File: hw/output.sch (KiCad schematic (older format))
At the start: 44 parts, among them J401 Conn_01x02, J402 Conn_01x02, J403 Conn_01x02, J404 Conn_01x02, J405 Conn_01x02, J406 Conn_01x02, J407 Conn_01x02, J408 Conn_01x02, J409 SERVO_OUT, J410 AUDIO, Q401 IRLML6344TRPBF, Q402 IRLML6344TRPBF, Q403 IRLML6344TRPBF, Q404 CSD17306Q5A, Q405 IRLML6344TRPBF, Q406 IRLML6344TRPBF, Q407 IRLML6344TRPBF, Q408 CSD17306Q5A, U401 MCP1416, U402 MCP1416, U403 AD5160BRJZ10-R2, U404 MCP6001-OT

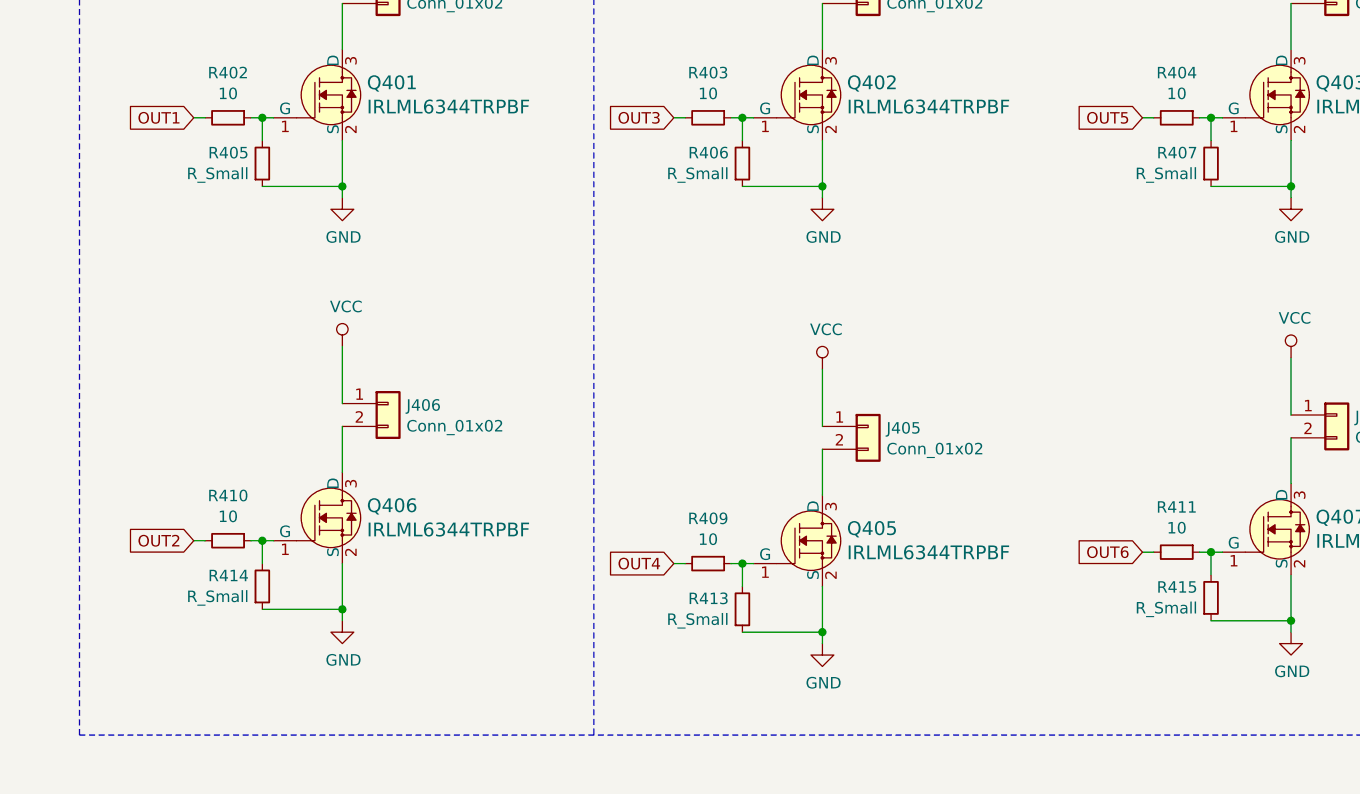
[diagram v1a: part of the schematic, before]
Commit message: Added cooling temperature sensor
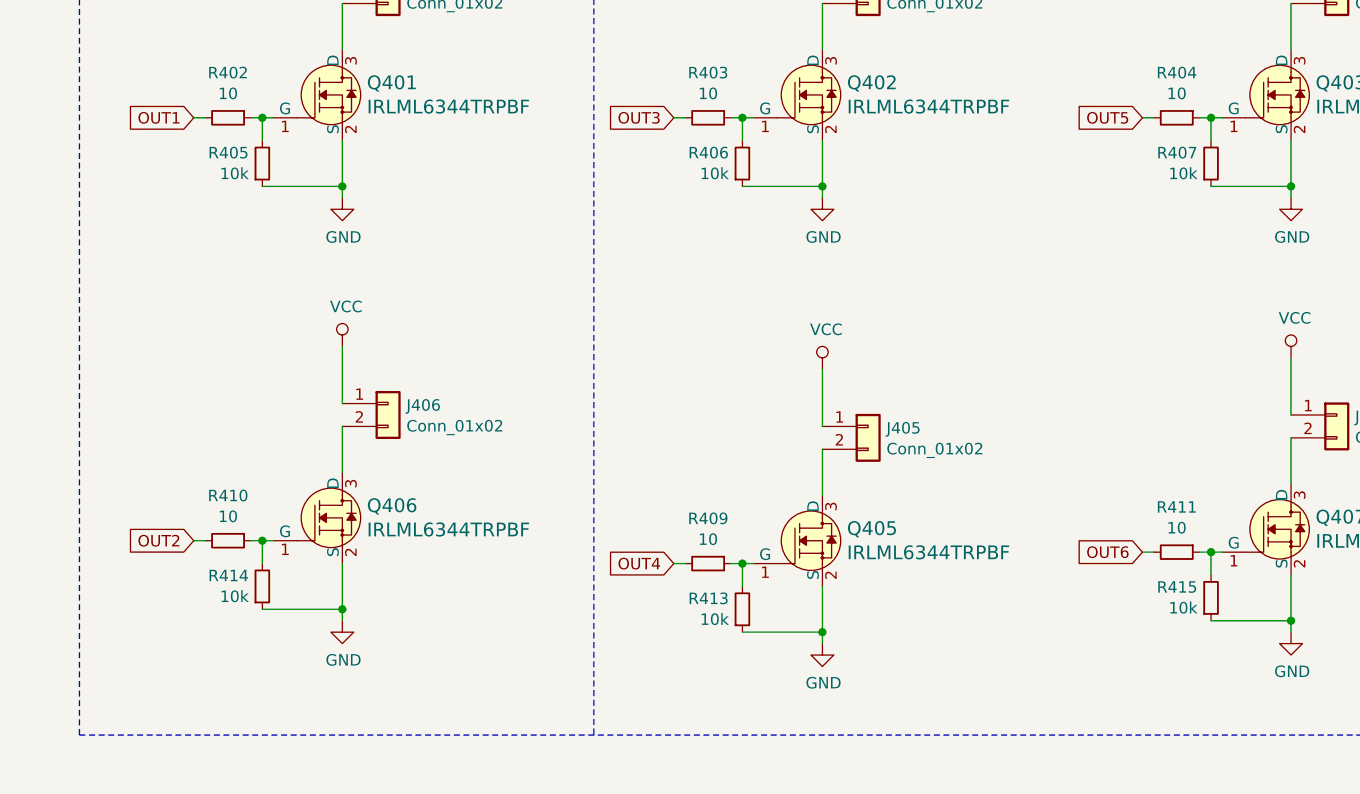
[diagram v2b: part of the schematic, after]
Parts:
- R405, R406, R407, R413, R414, R415: value R_Small -> 10k
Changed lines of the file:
@@
 P 5150 2000
 F 0 "R405" H 5091 1954 50  0000 R CNN
-F 1 "R_Small" H 5091 2045 50  0000 R CNN
+F 1 "10k" H 5091 2045 50  0000 R CNN
 F 2 "Resistors_SMD:R_0603_HandSoldering" H 5150 2000 50  0001 C CNN
 F 3 "~" H 5150 2000 50  0001 C CNN
@@
 P 7250 3950
 F 0 "R413" H 7191 3904 50  0000 R CNN
-F 1 "R_Small" H 7191 3995 50  0000 R CNN
+F 1 "10k" H 7191 3995 50  0000 R CNN
 F 2 "Resistors_SMD:R_0603_HandSoldering" H 7250 3950 50  0001 C CNN
 F 3 "~" H 7250 3950 50  0001 C CNN
@@
 P 7250 2000
 F 0 "R406" H 7191 1954 50  0000 R CNN
-F 1 "R_Small" H 7191 2045 50  0000 R CNN
+F 1 "10k" H 7191 2045 50  0000 R CNN
 F 2 "Resistors_SMD:R_0603_HandSoldering" H 7250 2000 50  0001 C CNN
 F 3 "~" H 7250 2000 50  0001 C CNN
@@
 P 5150 3850
 F 0 "R414" H 5091 3804 50  0000 R CNN
-F 1 "R_Small" H 5091 3895 50  0000 R CNN
+F 1 "10k" H 5091 3895 50  0000 R CNN
 F 2 "Resistors_SMD:R_0603_HandSoldering" H 5150 3850 50  0001 C CNN
 F 3 "~" H 5150 3850 50  0001 C CNN
@@
 P 9300 2000
 F 0 "R407" H 9241 1954 50  0000 R CNN
-F 1 "R_Small" H 9241 2045 50  0000 R CNN
+F 1 "10k" H 9241 2045 50  0000 R CNN
 F 2 "Resistors_SMD:R_0603_HandSoldering" H 9300 2000 50  0001 C CNN
 F 3 "~" H 9300 2000 50  0001 C CNN
@@
 P 9300 3900
 F 0 "R415" H 9241 3854 50  0000 R CNN
-F 1 "R_Small" H 9241 3945 50  0000 R CNN
+F 1 "10k" H 9241 3945 50  0000 R CNN
 F 2 "Resistors_SMD:R_0603_HandSoldering" H 9300 3900 50  0001 C CNN
 F 3 "~" H 9300 3900 50  0001 C CNN

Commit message: Added Opto-isolated inputs to the design Added uartdriver to the project Refined pin definitions
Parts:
- removed Q405, Q407: IRLML6344TRPBF, digikey-footprints:SOT-23-3, symbol dk_Transistors-FETs-MOSFETs-Single:IRLML6344TRPBF
- removed R413, R415: 10k, Resistors_SMD:R_0603_HandSoldering, symbol Device:R_Small
- added C407, C408: 100n, Capacitors_SMD:C_0603_HandSoldering, symbol Device:C_Small
- added U405, U406: TLP2361_TPL_E, digikey-footprints:SOIC-6-5_W4.55mm, symbol dk_Optoisolators-Logic-Output:TLP2361_TPL_E
- R409, R411: value 10 -> 100
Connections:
- net labels added: +3V3, HC_PWM1, HC_PWM2, IN1, IN2, PWM1, PWM2
- net labels removed: HC_OUT1, HC_OUT2, OUT3, OUT4, OUT5, OUT6
- wire segments 151 -> 157
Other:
- note added: "OPTO INPUTS"
- moved on the sheet: J403, J405, J407, Q403, R404, R407
